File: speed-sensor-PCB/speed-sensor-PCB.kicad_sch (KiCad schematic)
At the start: 9 parts, among them IC1 AS5600-ASOT, J1 Conn_01x01_Pin, J4 Conn_01x01_Pin, J5 Conn_01x01_Pin

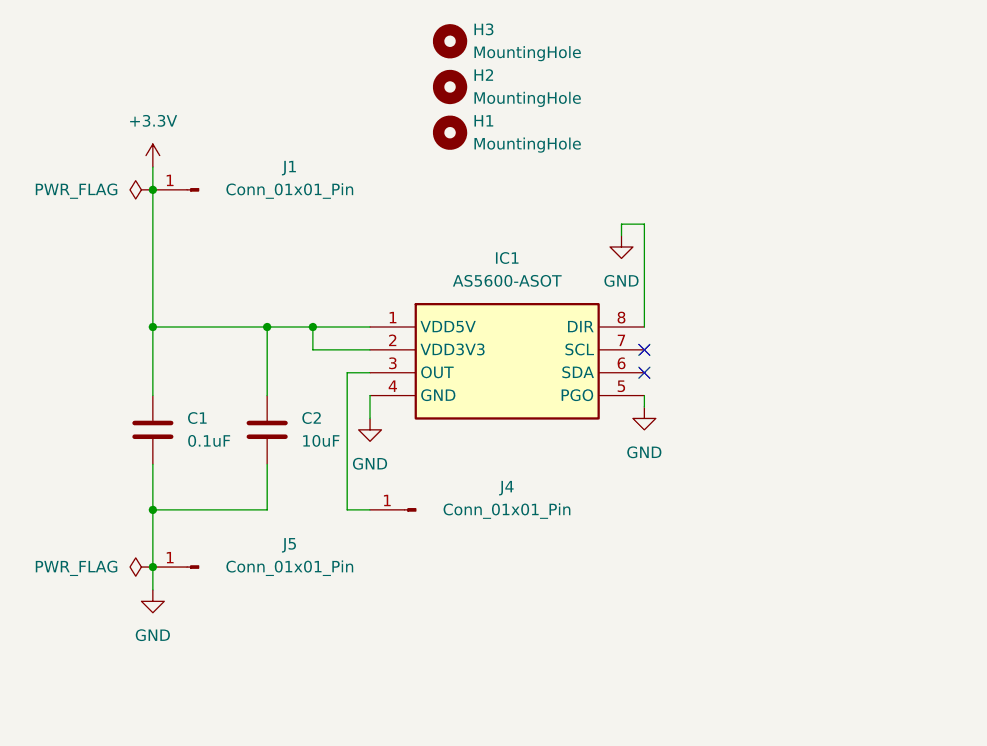
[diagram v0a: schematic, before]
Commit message: ordered JST VH and made speed sensor PCB design
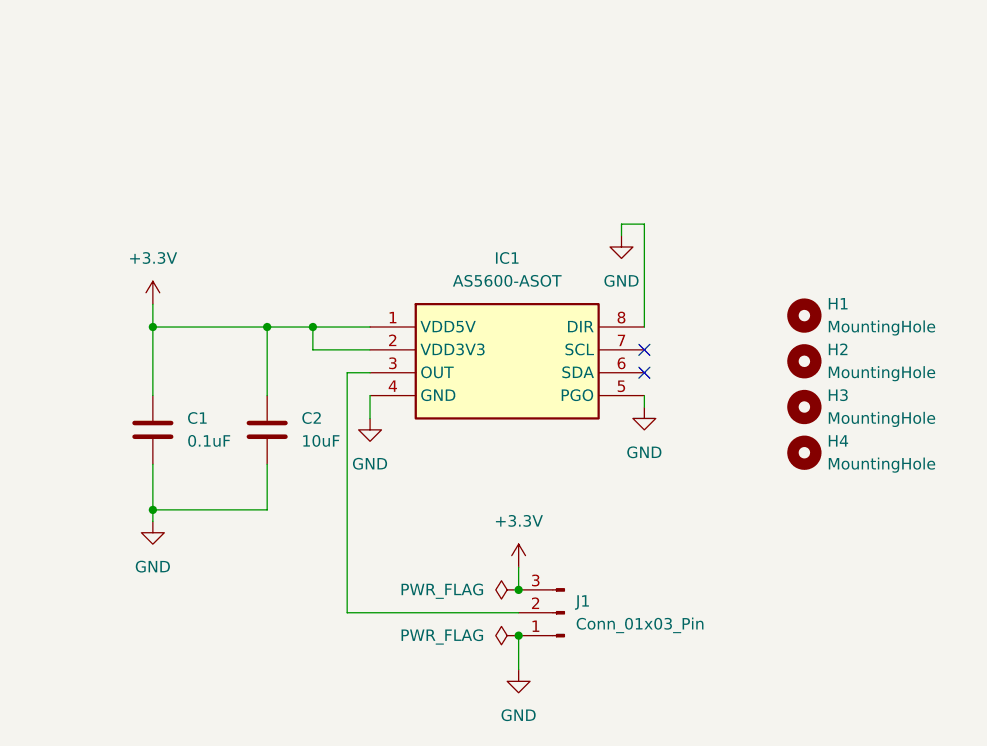
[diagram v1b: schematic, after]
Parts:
- removed J1, J4, J5: Conn_01x01_Pin, Connector_Wire:SolderWire-0.5sqmm_1x01_D0.9mm_OD2.1mm_Relief, symbol Connector:Conn_01x01_Pin
- added H4: MountingHole, MountingHole:MountingHole_3.2mm_M3_ISO7380, symbol Mechanical:MountingHole
- added J1: Conn_01x03_Pin, Connector_JST:JST_VH_B3P-VH-FB-B_1x03_P3.96mm_Vertical, symbol Connector:Conn_01x03_Pin
- H1, H2, H3: footprint MountingHole:MountingHole_6.4mm_M6_ISO14580 -> MountingHole:MountingHole_3.2mm_M3_ISO7380
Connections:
- net +3.3V: now also J1.3 (Pin_3)
- net GND: now also J1.1 (Pin_1)
- net at IC1.3 (OUT): now also J1.2 (Pin_2)
